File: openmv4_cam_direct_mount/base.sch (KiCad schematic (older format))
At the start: 58 parts, among them M1 9774030243R, M2 9774030243R, Q1 BSS138, Q2 Si2301BDS, U1 STM32H743VIT6, U5 TPS731XX, U8 PAM2305AABADJ, X1 MF-CON-MICROUSB-RIGHT, X2 USD-1040310811, X4 S2B-PH-K-S(LF)(SN)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

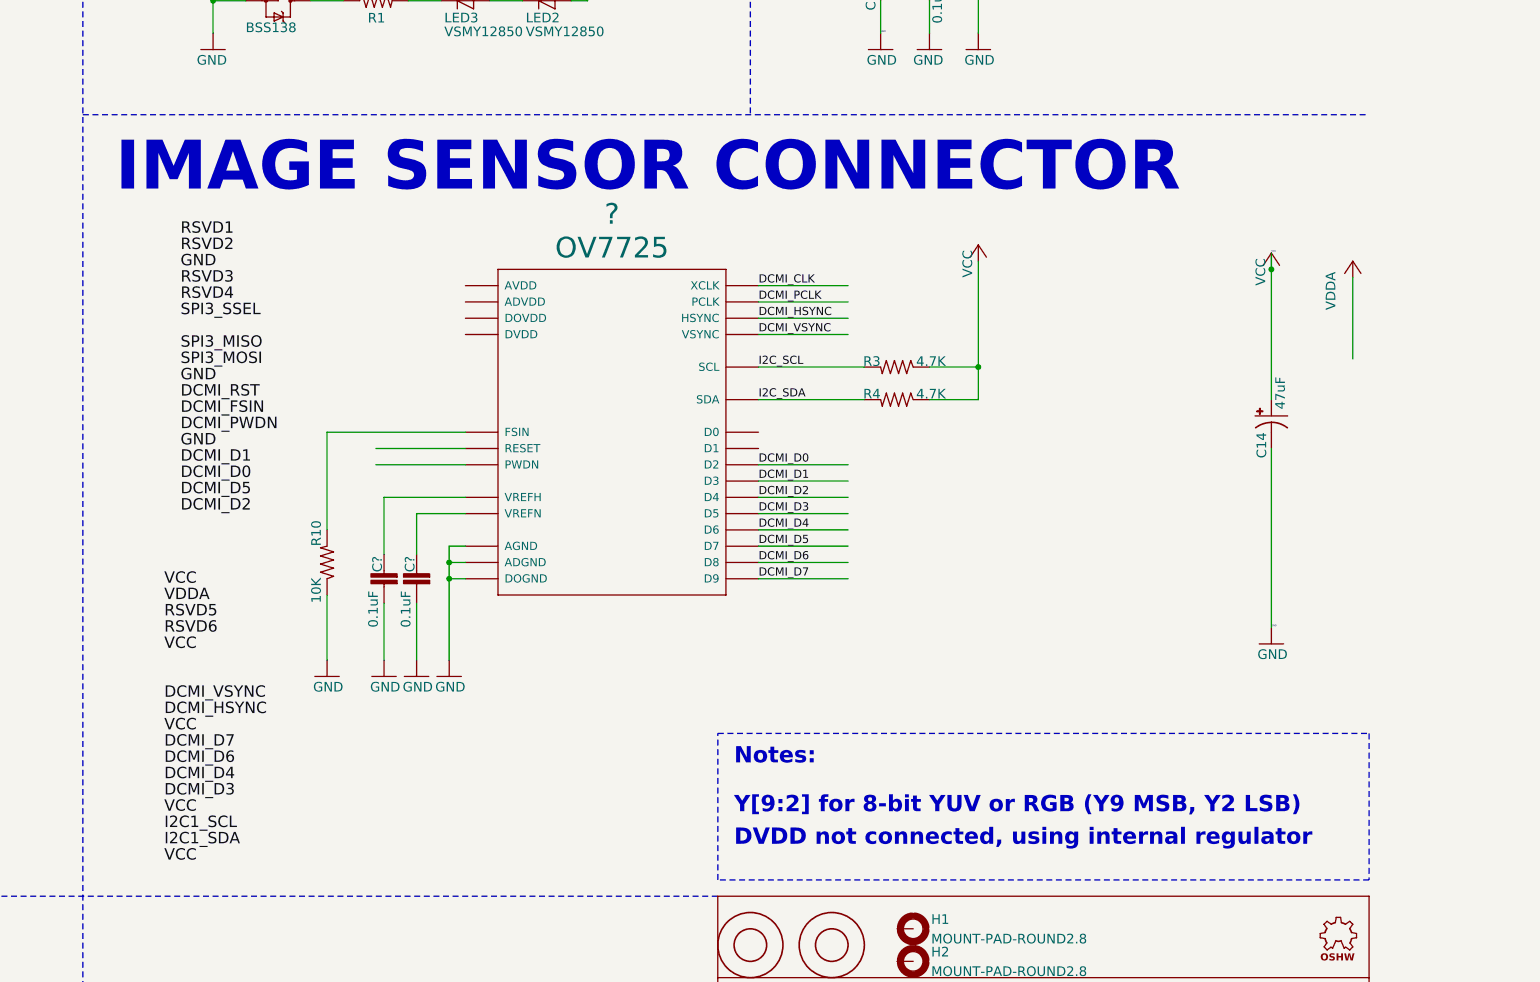
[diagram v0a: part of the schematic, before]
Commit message: More changes to direct mount schem
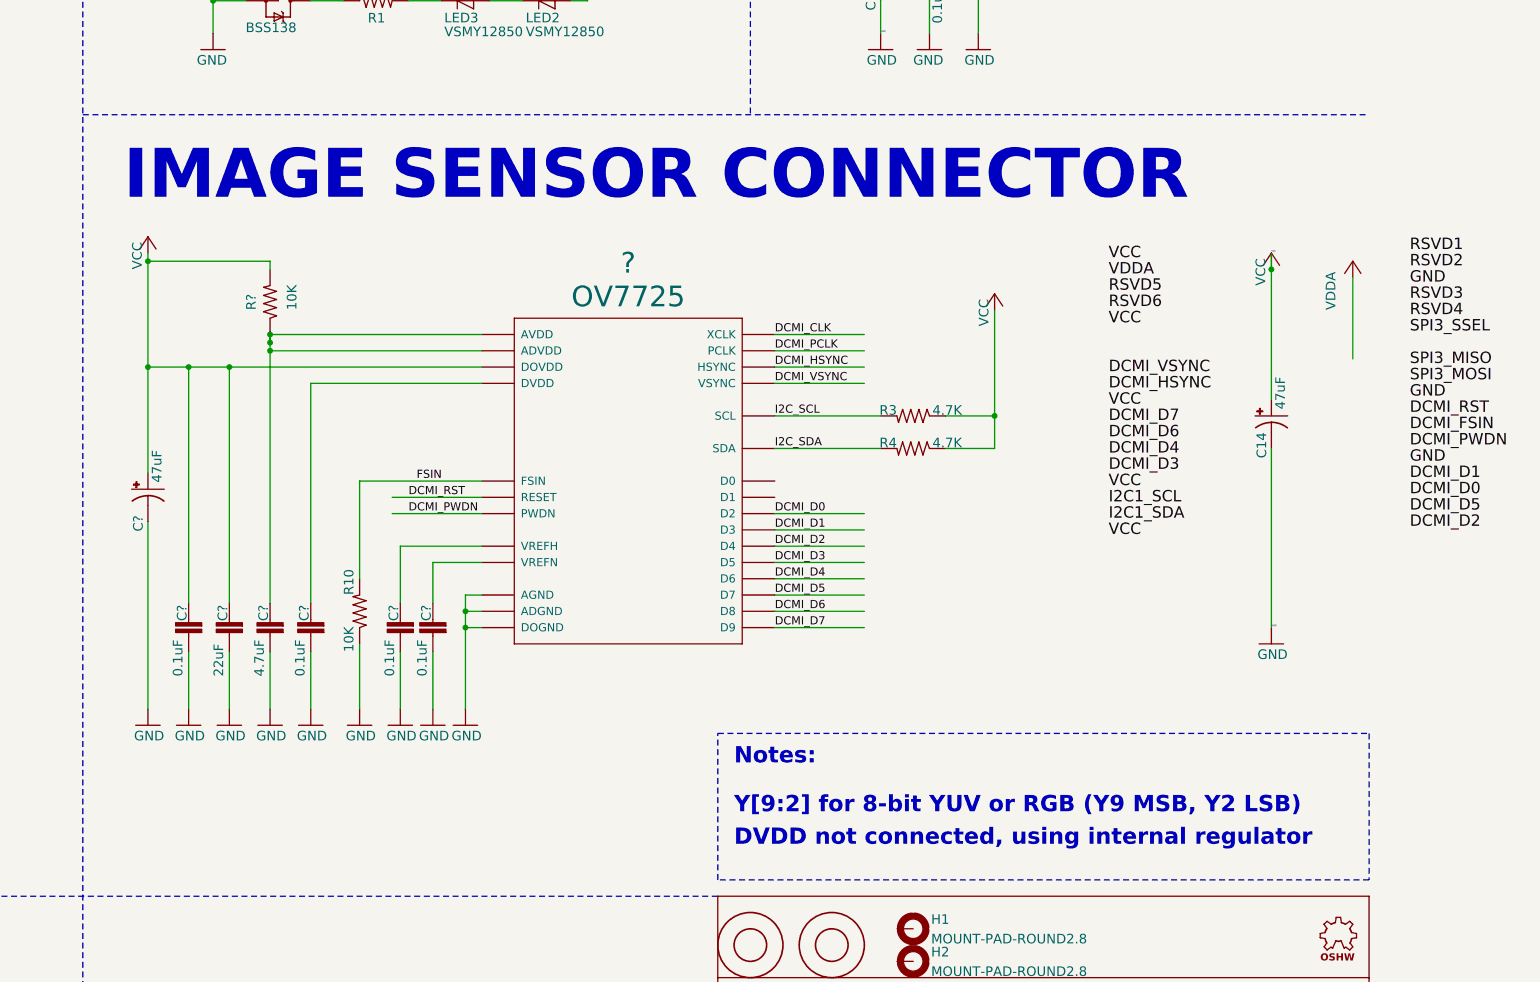
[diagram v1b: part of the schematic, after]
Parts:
- added C? (x2): 0.1uF, base:0603-CAP, symbol base-eagle-import:CAP0603-CAP
- added C?: 4.7uF, base:0603-CAP, symbol base-eagle-import:CAP0603-CAP
- added C?: 22uF, base:0603-CAP, symbol base-eagle-import:CAP0603-CAP
- added C?: 47uF, base:EIA3216, symbol base-eagle-import:CAP_POL1206
- added R?: 10K, base:0603-RES, symbol base-eagle-import:RESISTOR0603-RES
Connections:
- net labels added: FSIN
- wire segments 311 -> 333
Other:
- moved on the sheet: ?, C?, R10, R3, R4

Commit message: Listed more differences v3 to v4
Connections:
- net labels removed: FSIN, I2C_SCL, I2C_SDA
- wire segments 333 -> 332
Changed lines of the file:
@@
 U 1 1 F33451B3
 P 12200 4500
-F 0 "RN1" H 12120 4480 59  0000 L BNN
+F 0 "RN1" H 12100 4600 59  0000 L BNN
 F 1 "220R" H 12300 4380 59  0001 L BNN
 F 2 "base:EXBV8V" H 12200 4500 50  0001 C CNN
@@
 DCMI_VSYNC
 Text Label 15450 8550 0    50   ~ 0
-I2C_SCL
+I2C1_SCL
 Text Label 15450 8750 0    50   ~ 0
-I2C_SDA
+I2C1_SDA
 Text Label 15450 9150 0    50   ~ 0
 DCMI_D0
@@
 VCC
 Text Label 13250 8950 0    50   ~ 0
-FSIN
+DCMI_FSIN
 Text Label 13200 9050 0    50   ~ 0
 DCMI_RST
@@
 L base-eagle-import:VCC #P+?
 U 1 1 5E11A470
-P 11600 7450
-F 0 "#P+?" H 11600 7450 50  0001 C CNN
-F 1 "VCC" V 11700 7250 59  0000 L BNN
-F 2 "" H 11600 7450 50  0001 C CNN
-F 3 "" H 11600 7450 50  0001 C CNN
-	1    11600 7450
+P 11600 7350
+F 0 "#P+?" H 11600 7350 50  0001 C CNN
+F 1 "VCC" V 11750 7200 59  0000 L BNN
+F 2 "" H 11600 7350 50  0001 C CNN
+F 3 "" H 11600 7350 50  0001 C CNN
+	1    11600 7350
 	-1   0    0    -1
 $EndComp
 Wire Wire Line
 	13650 8250 12100 8250
-Wire Wire Line
-	11600 7550 11600 7600
 Connection ~ 11600 8250
 Wire Wire Line
@@
 	13650 8050 12350 8050
 Connection ~ 12350 8050
-Connection ~ 12350 8100
-Wire Wire Line
-	12350 8100 12350 8050
 Wire Wire Line
 	12350 7650 12350 7600
 Wire Wire Line
 	12350 7600 11600 7600
+Wire Wire Line
+	11600 7600 11600 8250
+Wire Wire Line
+	11600 7600 11600 7450
 Wire Wire Line
 	12350 8050 12350 8150
 Connection ~ 11600 7600
-Wire Wire Line
-	11600 7600 11600 8250
 $EndSCHEMATC
